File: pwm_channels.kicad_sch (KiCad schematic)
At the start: 0 parts

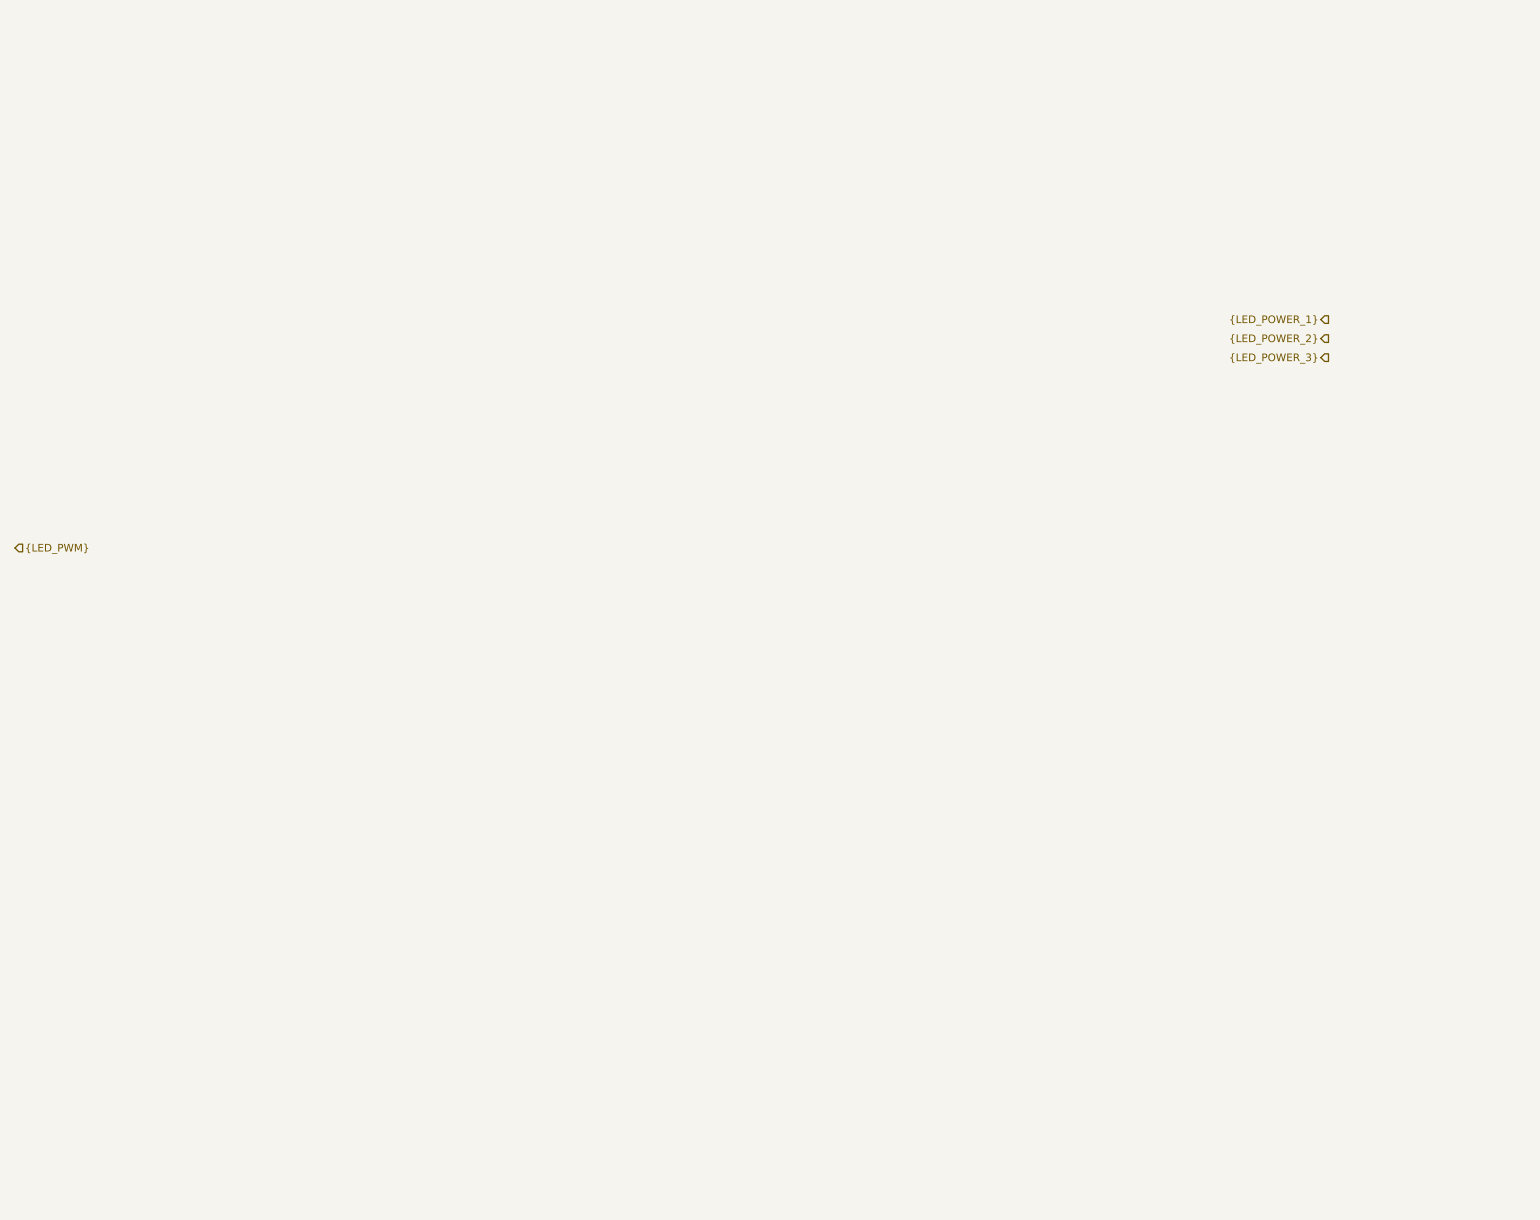
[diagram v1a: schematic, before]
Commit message: Add power stages
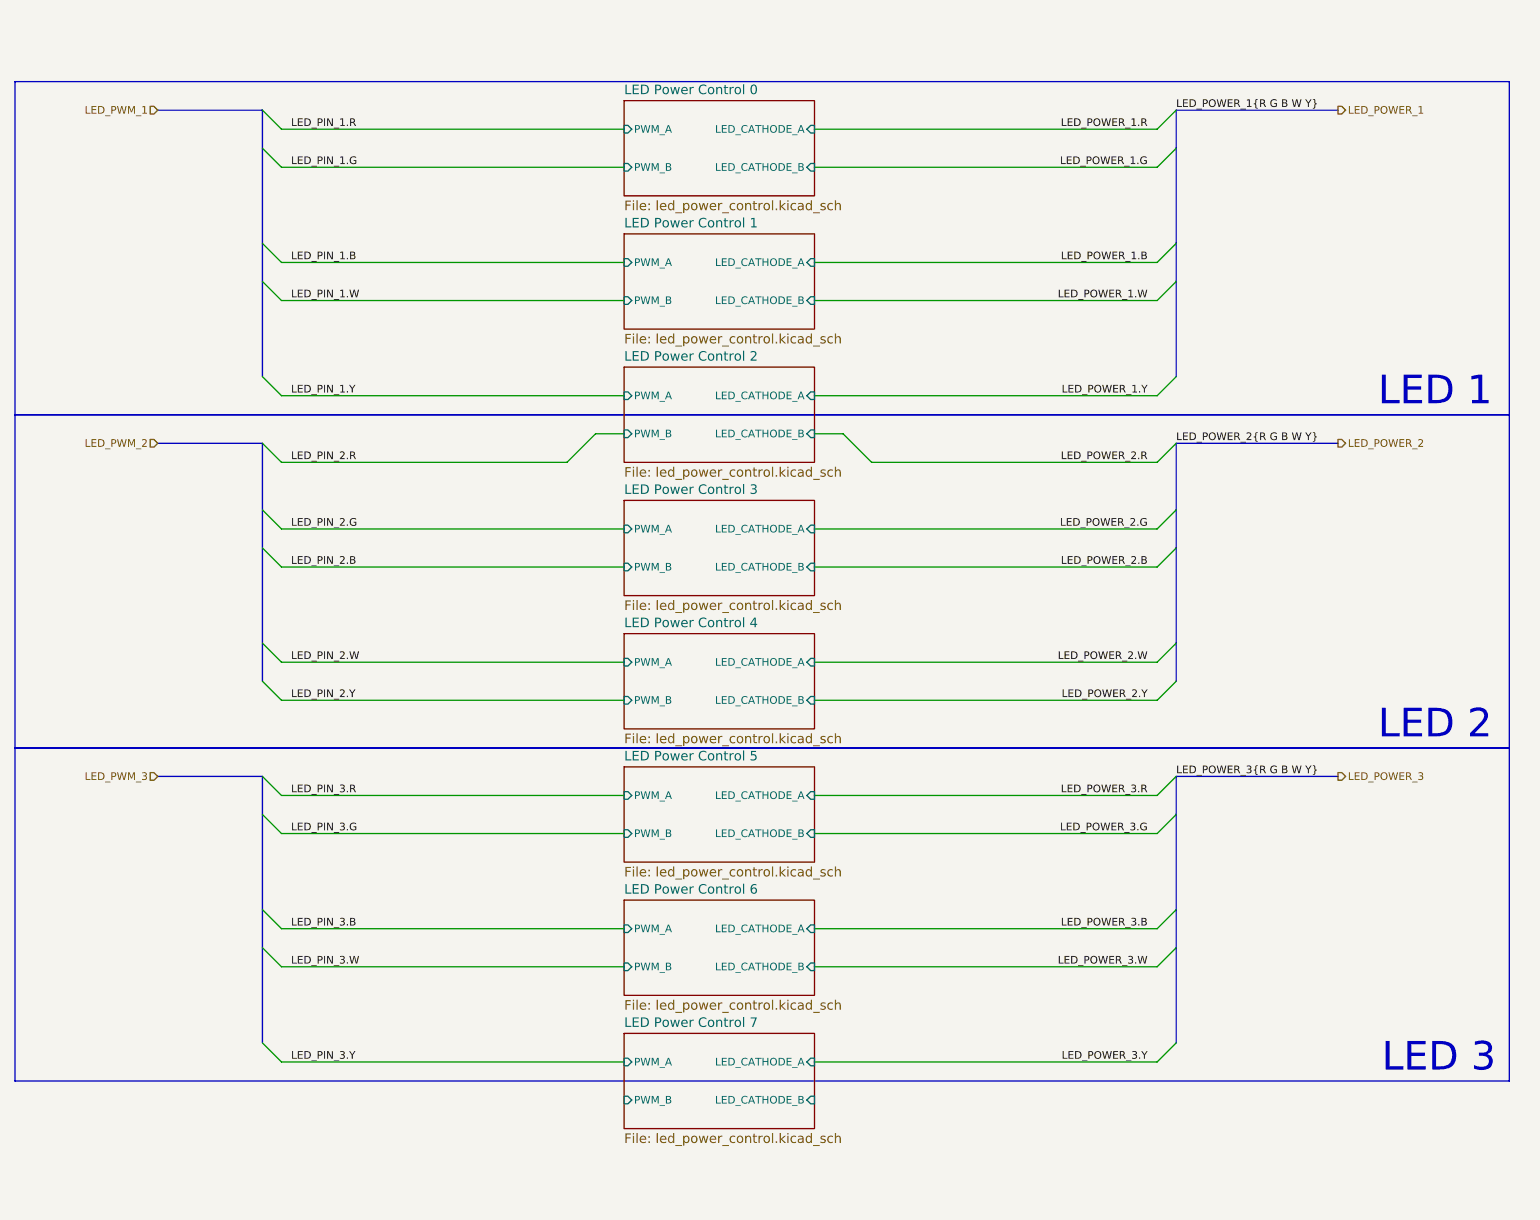
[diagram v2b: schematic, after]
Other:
- added sheet LED Power Control 0 (led_power_control.kicad_sch)
- added sheet LED Power Control 1 (led_power_control.kicad_sch)
- added sheet LED Power Control 2 (led_power_control.kicad_sch)
- added sheet LED Power Control 3 (led_power_control.kicad_sch)
- added sheet LED Power Control 4 (led_power_control.kicad_sch)
- added sheet LED Power Control 5 (led_power_control.kicad_sch)
- added sheet LED Power Control 6 (led_power_control.kicad_sch)
- added sheet LED Power Control 7 (led_power_control.kicad_sch)
- note added: "LED 1"
- note added: "LED 2"
- note added: "LED 3"

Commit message: Add power supplies
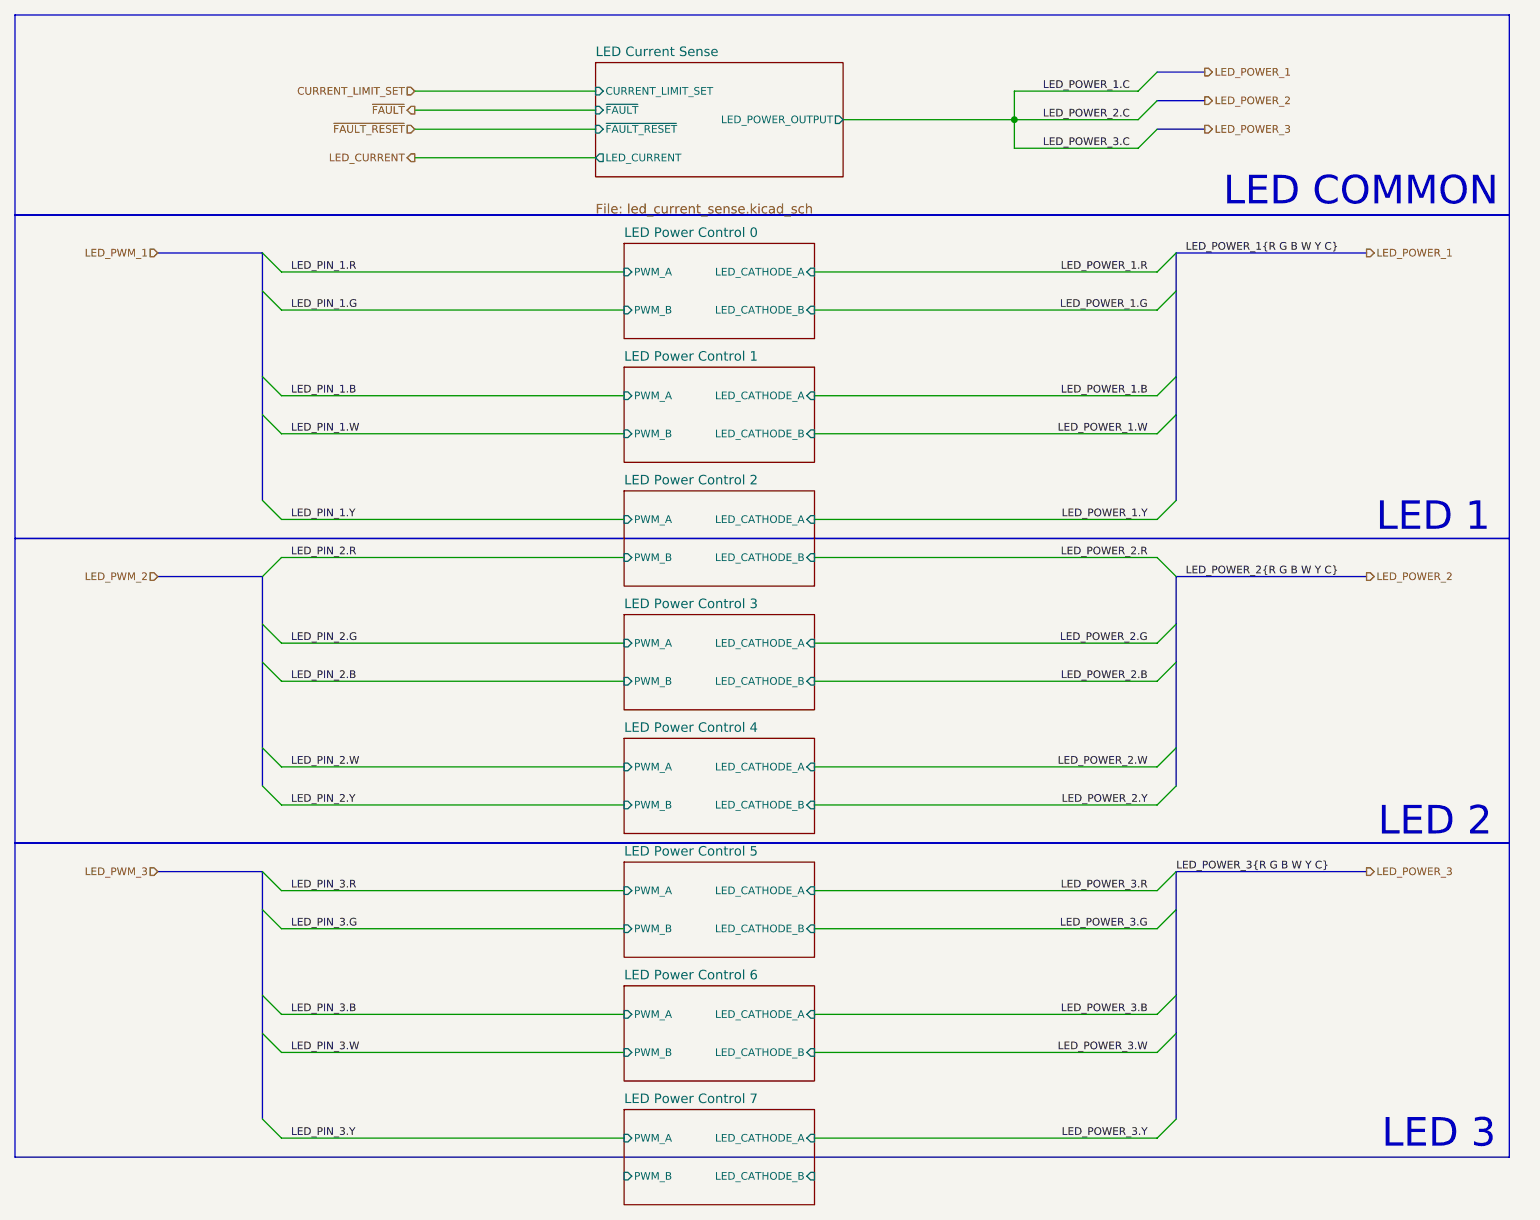
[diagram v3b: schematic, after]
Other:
- added sheet LED Current Sense (led_current_sense.kicad_sch)
- note added: "LED COMMON"
